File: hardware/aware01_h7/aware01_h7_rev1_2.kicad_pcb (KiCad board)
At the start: 4 copper layers, 77.5 x 110 mm, 177 parts, among them IC1 TLV320AIC3204IRHBR, J1 Conn_01x06_Pin, J10 CV2_IN, J11 V/OCT_IN, J12 CV1_IN, J2 Conn_01x03_Pin, J3 Conn_02x05_Odd_Even, J4 InL, J5 InR, J6 OutL, J7 OutR, J8 GATE1_IN, J9 GATE2_IN, Q1 MMBT3904, Q2 MMBT3904, SW1 SW_Push, SW2 SW_Push, SW3 SW_Push, U1 STM32H7B0ZBTx, U10 NE5532DRG4, U11 LMV722IDR, U12 LMV722IDR, U2 IS45S16800F-7TLA2, U3 10k, U4 10k, U5 10k, U6 10k, U7 LM1117MP-3.3, U8 LM4040DIM3X-10, U9 NE5532DRG4, Y1 WE-XTAL 24.0MHz 50ppm

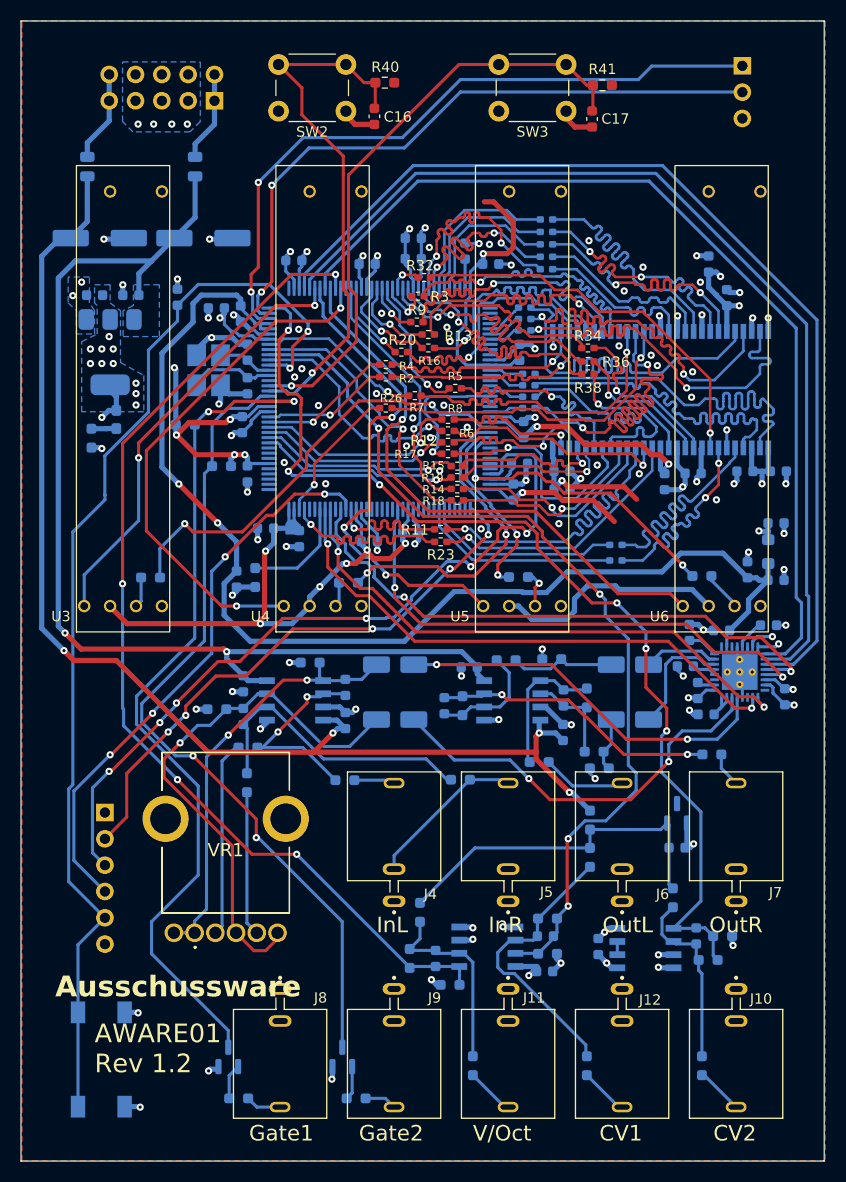
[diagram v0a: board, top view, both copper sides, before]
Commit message: add 3rd Gate In and add resistor part No's
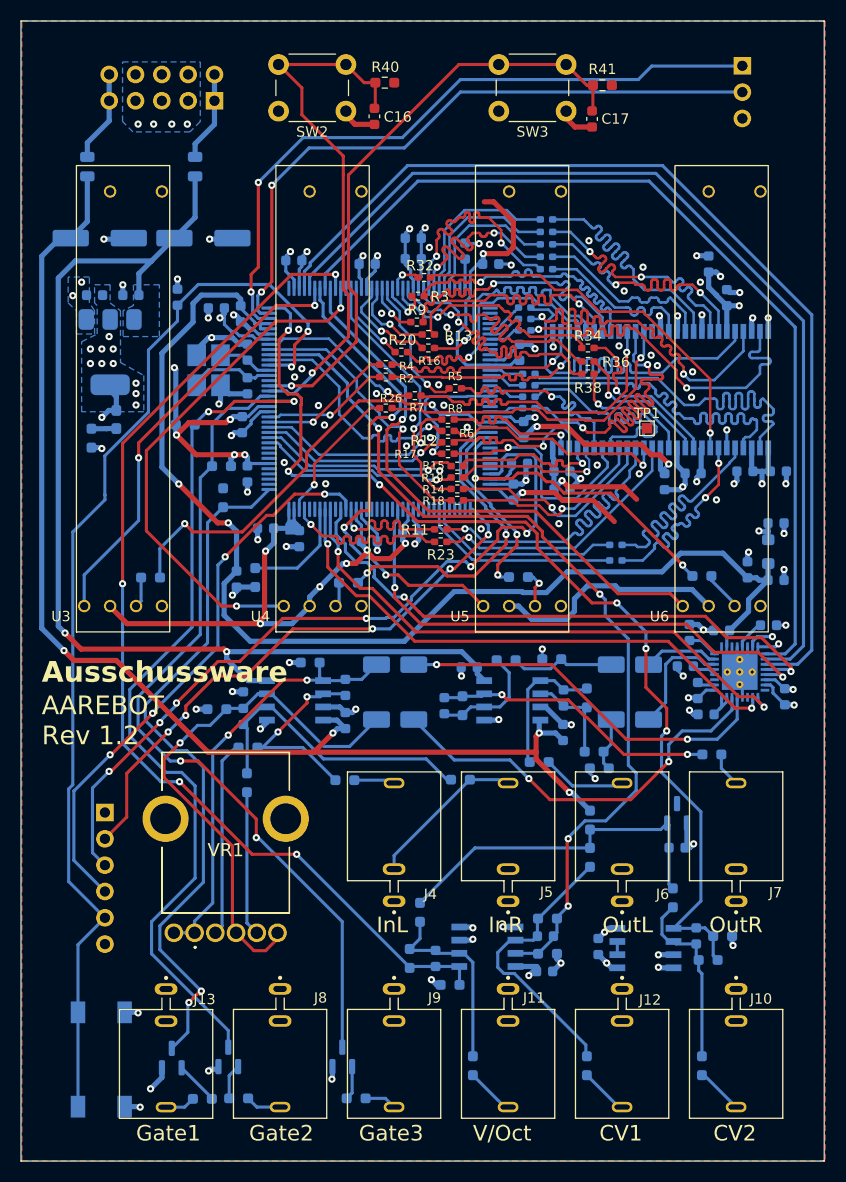
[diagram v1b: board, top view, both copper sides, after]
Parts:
- added J13: GATE3_IN, Eurorack:THONK_PJ398SM-12, F.Cu at (129.5, 140.9)
- added Q3: MMBT3904, Package_TO_SOT_SMD:SOT-23, B.Cu at (130.1, 141.1)
- added R78: 100k, Resistor_SMD:R_0603_1608Metric_Pad0.98x0.95mm_HandSolder, B.Cu at (133.0, 145.0)
- added R79: 10k, Resistor_SMD:R_0603_1608Metric_Pad0.98x0.95mm_HandSolder, B.Cu at (135.0, 87.0)
- added TP1: FMC_SDCLK, TestPoint:TestPoint_Pad_1.0x1.0mm, F.Cu at (175.9, 80.3)
- R46: value 150 -> 1k
- U1: value STM32H7B0ZBTx -> STM32H750ZBT6
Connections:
- U1 pad 1: unconnected-(U1-PE2-Pad1) -> /GATE3_IN
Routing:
- net /GATE3_IN: track 0.00 -> 68.1 mm, vias 0 -> 2
- net Net-(Q3-B): track 0.00 -> 4.21 mm
- net Net-(J13-PadT): track 0.00 -> 3.12 mm
- net GND: track 171.2 -> 173.7 mm, vias 111 -> 112
- net /V_OCT_IN: track 99.9 -> 100.9 mm
- net /GATE2_IN: track 78.7 -> 79.6 mm
- net /GATE1_IN: track 83.0 -> 83.8 mm
- net +3.3VA: track 113.7 -> 114.3 mm
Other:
- board text added: "AAREBOT Rev 1.2"
- board text added: "Gate3"
- board text removed: "AWARE01 Rev 1.2"

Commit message: slight changes to layout
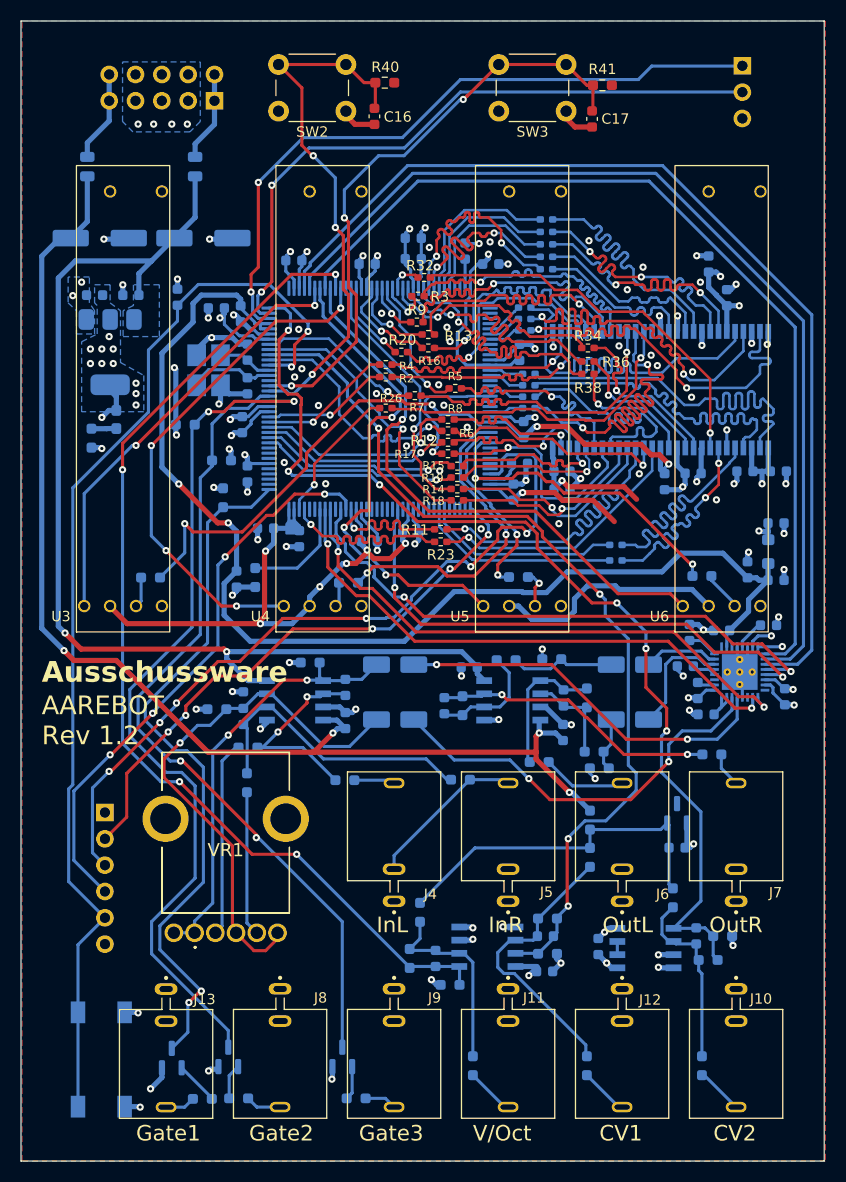
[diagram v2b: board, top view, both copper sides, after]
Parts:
- removed TP1: FMC_SDCLK, TestPoint:TestPoint_Pad_1.0x1.0mm
- moved R65 0.55 mm to (134.8, 83.4)
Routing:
- net +3.3V: track 245.7 -> 223.1 mm, vias 40 -> 41
- net GND: track 173.7 -> 170.7 mm
- net Net-(C51-Pad1): track 52.9 -> 51.7 mm
- net /GATE2_IN: track 79.6 -> 78.7 mm
- net /UART4_TX: track 66.7 -> 66.1 mm
- net /FAD_LED4_OUT: track 29.9 -> 30.5 mm
- net /BUTTON2_IN: track 58.2 -> 57.6 mm, vias 1 -> 3
- net /FADER2_IN: track 50.4 -> 50.0 mm, vias 2 -> 4
- net /BUTTON1_IN: track 51.8 -> 51.9 mm, vias 1 -> 3

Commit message: length matching incl. termination resistors
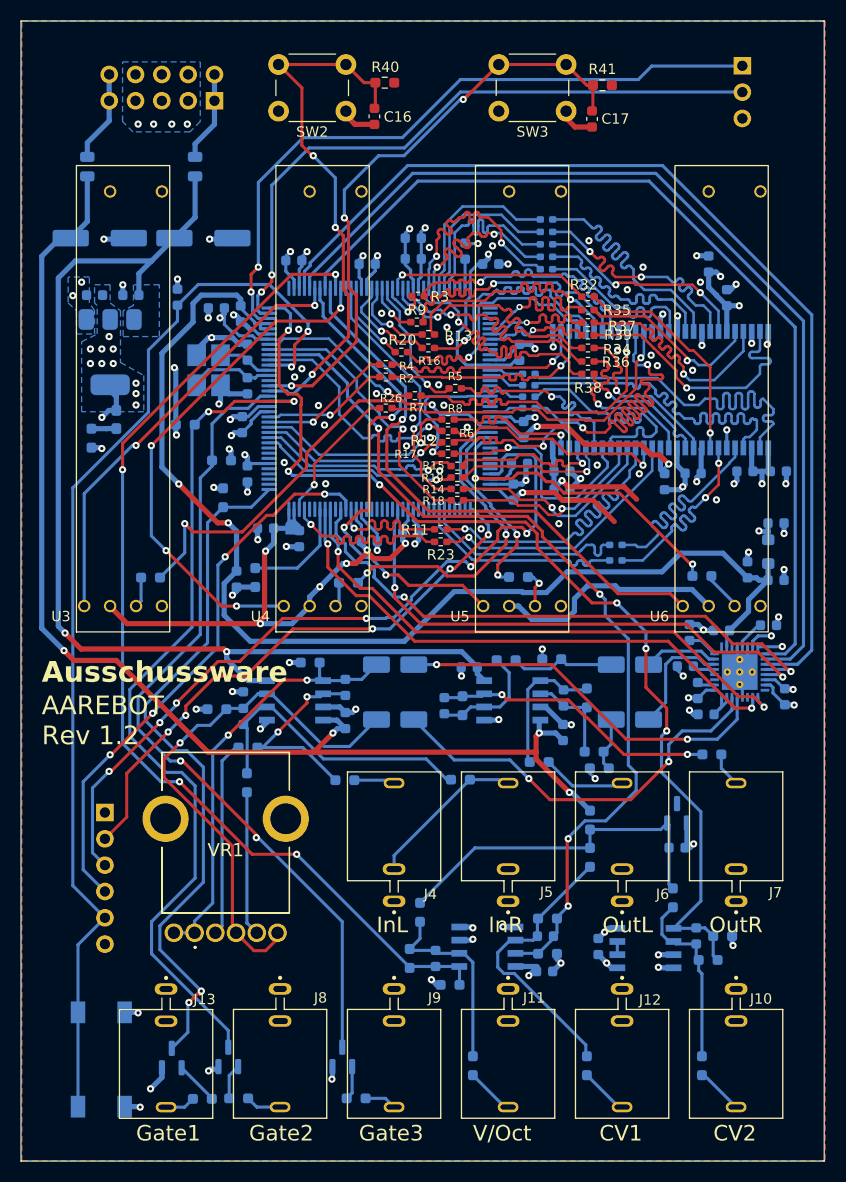
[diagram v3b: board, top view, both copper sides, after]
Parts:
- R35, R37, R39: moved to F.Cu
- moved R32 15.9 mm to (170.2, 67.6)
- moved R39 6.12 mm to (170.2, 71.3)
- moved R37 6.11 mm to (170.2, 70.1)
- moved R35 6.10 mm to (170.2, 68.9)
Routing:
- net Net-(U2-DQ13): track 40.0 -> 18.6 mm, vias 0 -> 1
- net /FMC_D4: track 3.08 -> 19.7 mm
- net Net-(U2-DQ4): track 37.9 -> 21.8 mm
- net Net-(U2-DQ14): track 37.0 -> 23.6 mm, vias 2 -> 1
- net /FMC_D13: track 3.66 -> 16.1 mm, vias 0 -> 1
- net Net-(U2-DQ15): track 37.6 -> 26.5 mm, vias 2 -> 1
- net /FMC_D14: track 3.34 -> 12.4 mm, vias 0 -> 1
- net /FMC_D15: track 3.09 -> 11.6 mm, vias 0 -> 1
- net Net-(U2-DQ12): track 26.0 -> 20.8 mm
- net /FMC_D12: track 14.4 -> 19.5 mm
- net Net-(U2-DQ9): track 18.1 -> 21.2 mm
- net Net-(U2-DQ6): track 13.9 -> 16.8 mm
- net /FMC_D9: track 21.7 -> 19.4 mm
- net Net-(U2-DQ2): track 25.2 -> 23.2 mm
- net Net-(U2-DQ3): track 21.7 -> 19.8 mm
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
